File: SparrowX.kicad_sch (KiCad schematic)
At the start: 27 parts, among them J1 NORTH, J2 SOUTH, J3 WEST, J4 EAST, U1 TPS629210-Q1, U2 LD49100PU33RY, U3 STM32G0B1CBU6, U4 TCAN332G, U5 TCAN332G

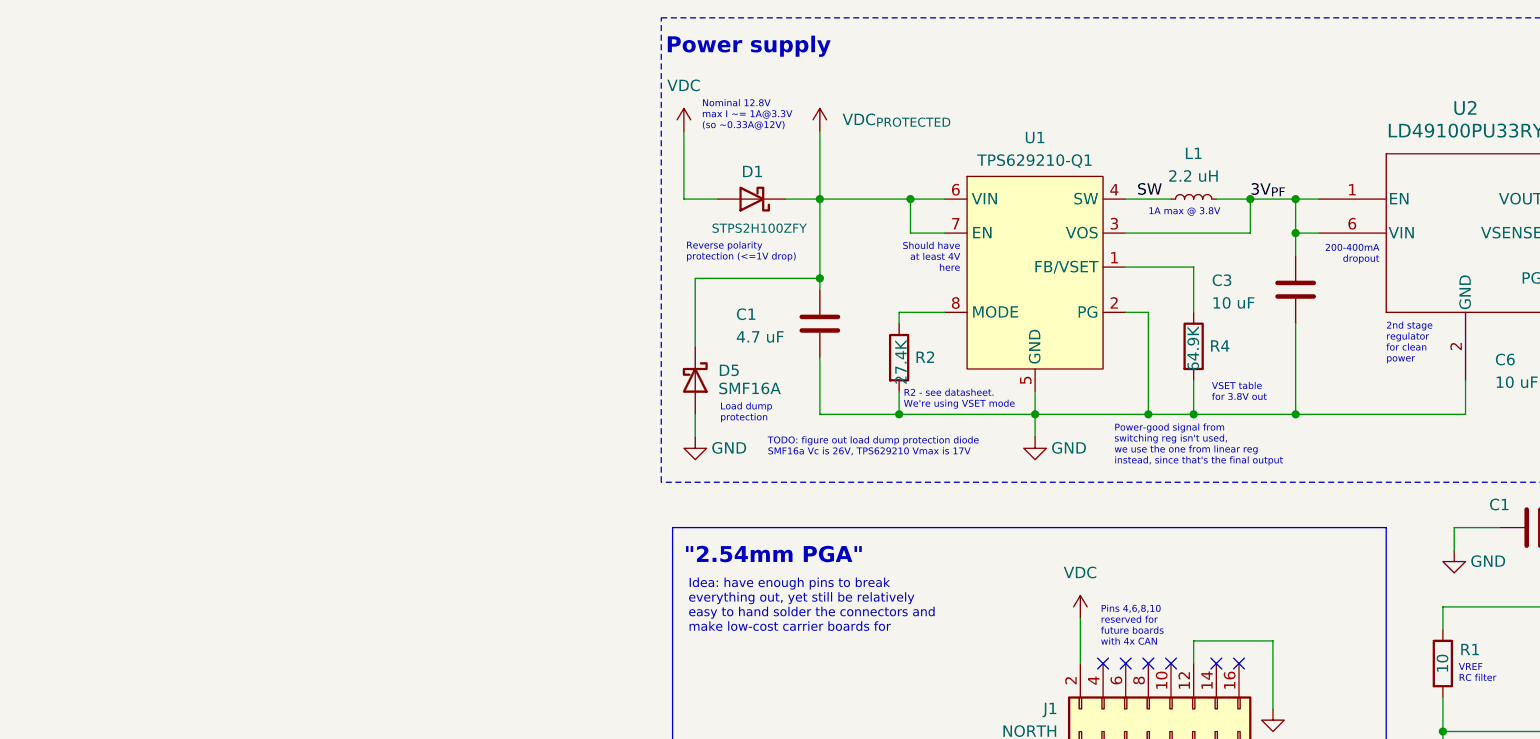
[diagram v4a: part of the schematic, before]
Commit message: WIP: new switching regulator
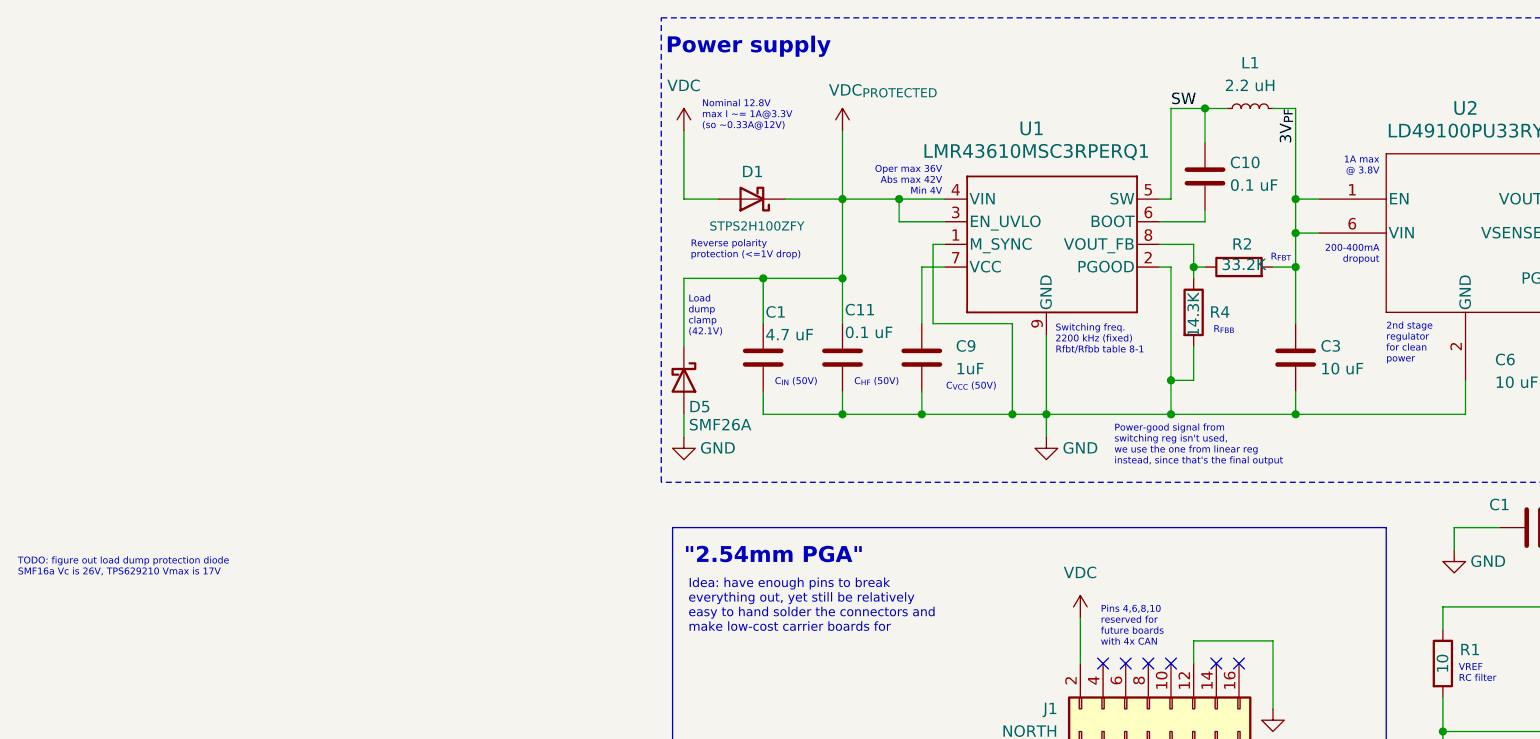
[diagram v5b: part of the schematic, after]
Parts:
- removed U1: TPS629210-Q1, Package_TO_SOT_SMD:SOT-583-8, symbol SparrowX-Components-Library:TPS629210
- added C10, C11: 0.1 uF, Capacitor_SMD:C_0402_1005Metric, symbol Device:C
- added C9: 1uF, Capacitor_SMD:C_0402_1005Metric, symbol Device:C
- added U1: LMR43610MSC3RPERQ1, footprint:RPE0009A-MFG, symbol LMR43610MSC5RPERQ1:LMR43610MSC5RPERQ1
- C3: footprint Capacitor_SMD:C_0805_2012Metric -> Capacitor_SMD:C_0402_1005Metric
- D5: value SMF16A -> SMF26A
- R2: value 27.4K -> 33.2K
- R4: value 64.9K -> 14.3K
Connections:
- net 3V_{PF}: now also R2.2
- net GND: now also C11.2, C9.2, U1.1 (M_SYNC), U1.2 (PGOOD), U1.9 (GND); no longer R2.2
- net SW: now also C10.2, U1.5 (SW)
- net VDC_{PROTECTED}: now also C11.1, U1.3 (EN_UVLO), U1.4 (VIN)
- net at R4.1: now also R2.1, U1.8 (VOUT_FB)
- new net: C10.1, U1.6 (BOOT)
- new net: C9.1, U1.7 (VCC)
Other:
- note added: "C_{HF} (50V)"
- note added: "C_{IN} (50V)"
- note added: "C_{VCC} (50V)"
- note added: "Load dump clamp (42.1V)"
- note added: "Oper max 36V Abs max 42V Min 4V"
- note added: "R_{FBB}"
- note added: "R_{FBT}"
- note added: "Switching freq. 2200 kHz (fixed) Rfbt/Rfbb table 8-1"
- note removed: "Load dump protection"
- note removed: "R2 - see datasheet. We're using VSET mode"
- note removed: "Should have at least 4V here"
- note removed: "VSET table for 3.8V out"
- moved on the sheet: C1, C3, D5, L1, R2, R4

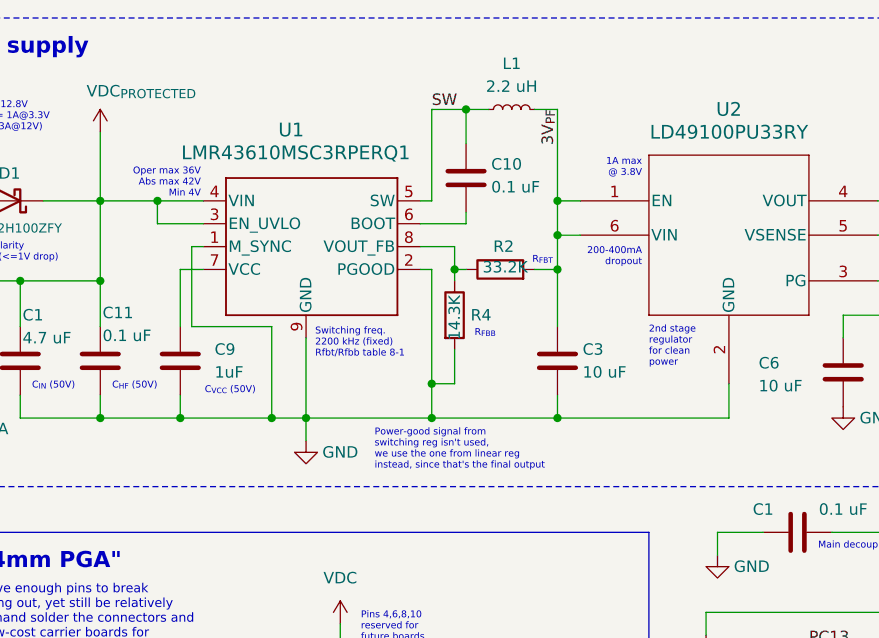
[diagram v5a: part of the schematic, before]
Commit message: PSU P1 migration done!
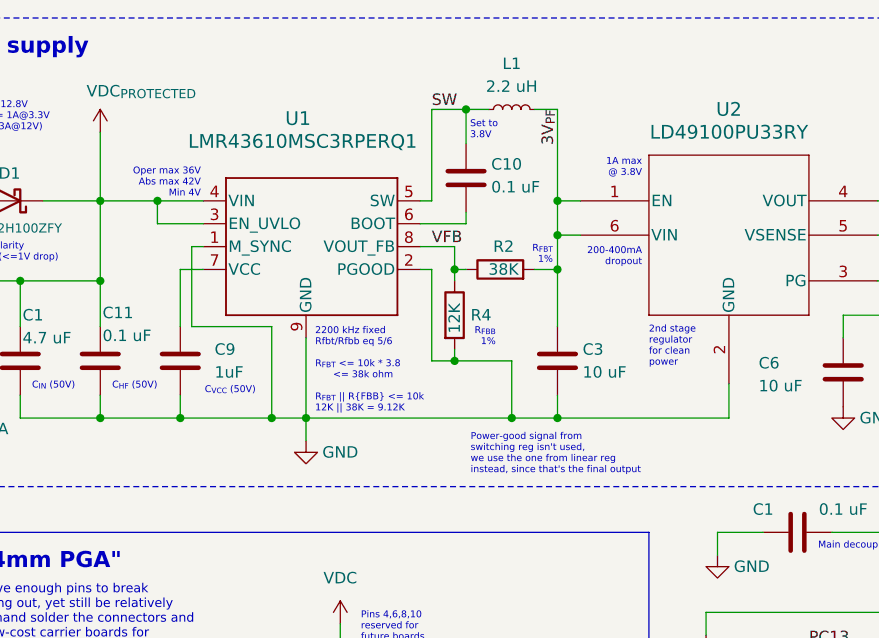
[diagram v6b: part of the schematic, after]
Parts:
- R2: value 33.2K -> 38K
- R4: value 14.3K -> 12K
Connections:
- net VFB: now reaches R2.1, R4.1, U1.8 (VOUT_FB)
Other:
- note added: "2200 kHz fixed Rfbt/Rfbb eq 5/6 R_{FBT} <= 10k * 3.8 <= 38k ohm R_{FBT} || R{FBB} <= 10k 12K || 38K = 9.12K"
- note added: "R_{FBB} 1%"
- note added: "R_{FBT} 1%"
- note added: "Set to 3.8V"
- note removed: "R_{FBB}"
- note removed: "R_{FBT}"
- note removed: "Switching freq. 2200 kHz (fixed) Rfbt/Rfbb table 8-1"
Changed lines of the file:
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@@
 	)
 	(junction
+		(at 72.39 50.8)
+		(diameter 0)
+		(color 0 0 0 0)
+	)
+	(junction
 		(at 123.19 45.72)
 		(diameter 0)
@@
 	)
 	(junction
-		(at 69.85 53.34)
-		(diameter 0)
-		(color 0 0 0 0)
-	)
-	(junction
 		(at 72.39 40.64)
 		(diameter 0)
@@
 	)
 	(junction
+		(at 78.74 57.15)
+		(diameter 0)
+		(color 0 0 0 0)
+	)
+	(junction
 		(at 27.94 130.81)
 		(diameter 0)
@@
 	)
 	(junction
-		(at 69.85 57.15)
-		(diameter 0)
-		(color 0 0 0 0)
-	)
-	(junction
 		(at 232.41 113.03)
 		(diameter 0)
@@
 	(wire
 		(pts
+			(xy 72.39 50.8) (xy 78.74 50.8)
+		)
+		(stroke
+			(width 0)
+			(type default)
+		)
+	)
+	(wire
+		(pts
+			(xy 69.85 50.8) (xy 72.39 50.8)
+		)
+		(stroke
+			(width 0)
+			(type default)
+		)
+	)
+	(wire
+		(pts
 			(xy 45.72 180.34) (xy 45.72 189.23)
 		)
@@
 		)
 	)
+	(wire
+		(pts
+			(xy 78.74 50.8) (xy 78.74 57.15)
+		)
+		(stroke
+			(width 0)
+			(type default)
+		)
+	)
 	(bus
 		(pts
@@
 	(wire
 		(pts
-			(xy 55.88 57.15) (xy 69.85 57.15)
-		)
-		(stroke
-			(width 0)
-			(type default)
-		)
-	)
-	(wire
-		(pts
 			(xy 119.38 36.83) (xy 123.19 36.83)
 		)
@@
 	(wire
 		(pts
-			(xy 69.85 53.34) (xy 69.85 57.15)
-		)
-		(stroke
-			(width 0)
-			(type default)
-		)
-	)
-	(wire
-		(pts
 			(xy 72.39 38.1) (xy 72.39 40.64)
 		)
@@
 	(wire
 		(pts
+			(xy 78.74 57.15) (xy 83.82 57.15)
+		)
+		(stroke
+			(width 0)
+			(type default)
+		)
+	)
+	(wire
+		(pts
 			(xy 160.02 121.92) (xy 160.02 135.89)
 		)
@@
 	(wire
 		(pts
-			(xy 72.39 53.34) (xy 69.85 53.34)
-		)
-		(stroke
-			(width 0)
-			(type default)
-		)
-	)
-	(wire
-		(pts
 			(xy 41.91 40.64) (xy 41.91 46.99)
 		)
@@
 	(wire
 		(pts
-			(xy 69.85 57.15) (xy 83.82 57.15)
+			(xy 55.88 57.15) (xy 78.74 57.15)
 		)
 		(stroke
@@
 	(wire
 		(pts
-			(xy 72.39 49.53) (xy 72.39 53.34)
+			(xy 72.39 49.53) (xy 72.39 50.8)
 		)
 		(stroke
@@
 	(wire
 		(pts
-			(xy 69.85 40.64) (xy 69.85 53.34)
+			(xy 69.85 40.64) (xy 69.85 50.8)
 		)
 		(stroke
@@
 		)
 	)
-	(text "Switching freq.\n2200 kHz (fixed)\nRfbt/Rfbb table 8-1"
+	(text "2200 kHz fixed\nRfbt/Rfbb eq 5/6\n\nR_{FBT} <= 10k * 3.8\n      <= 38k ohm\n\nR_{FBT} || R{FBB} <= 10k\n12K || 38K = 9.12K\n"
 		(exclude_from_sim no)
-		(at 56.896 50.546 0)
+		(at 56.896 56.642 0)
 		(effects
 			(font
@@
 	(text "Power-good signal from\nswitching reg isn't used,\nwe use the one from linear reg\ninstead, since that's the final output"
 		(exclude_from_sim no)
-		(at 63.5 62.992 0)
+		(at 74.168 63.5 0)
 		(effects
 			(font
@@
 		)
 	)
-	(text "R_{FBB}"
+	(text "R_{FBB}\n1%"
 		(exclude_from_sim no)
-		(at 76.962 48.26 0)
+		(at 76.962 49.276 0)
 		(effects
 			(font
@@
 		)
 	)
+	(text "Set to\n3.8V"
+		(exclude_from_sim no)
+		(at 74.1117 26.288 0)
+		(effects
+			(font
+				(size 0.762 0.762)
+			)
+			(justify left bottom)
+		)
+	)
 	(text "USB ESD\nProtection"
 		(exclude_from_sim no)
@@
 		)
 	)
-	(text "R_{FBT}"
+	(text "R_{FBT}\n1%"
 		(exclude_from_sim no)
 		(at 83.312 40.132 0)
@@
 		)
 	)
+	(label "VFB"
+		(at 69.85 38.1 0)
+		(fields_autoplaced yes)
+		(effects
+			(font
+				(size 1.27 1.27)
+			)
+			(justify left bottom)
+		)
+	)
 	(label "PA0"
 		(at 43.18 189.23 90)
@@
 			)
 		)
-		(property "Value" "14.3K"
-			(at 72.39 48.514 90)
+		(property "Value" "12K"
+			(at 72.39 47.752 90)
 			(effects
 				(font
@@
 		(dnp no)
 		(property "Reference" "U1"
-			(at 54.229 25.146 0)
+			(at 54.991 23.876 0)
 			(effects
 				(font
@@
 		)
 		(property "Value" "LMR43610MSC3RPERQ1"
-			(at 54.737 27.686 0)
+			(at 55.499 26.416 0)
 			(effects
 				(font
@@
 			)
 		)
-		(property "Value" "33.2K"
-			(at 80.518 40.386 90)
+		(property "Value" "38K"
+			(at 79.502 40.64 90)
 			(effects
 				(font

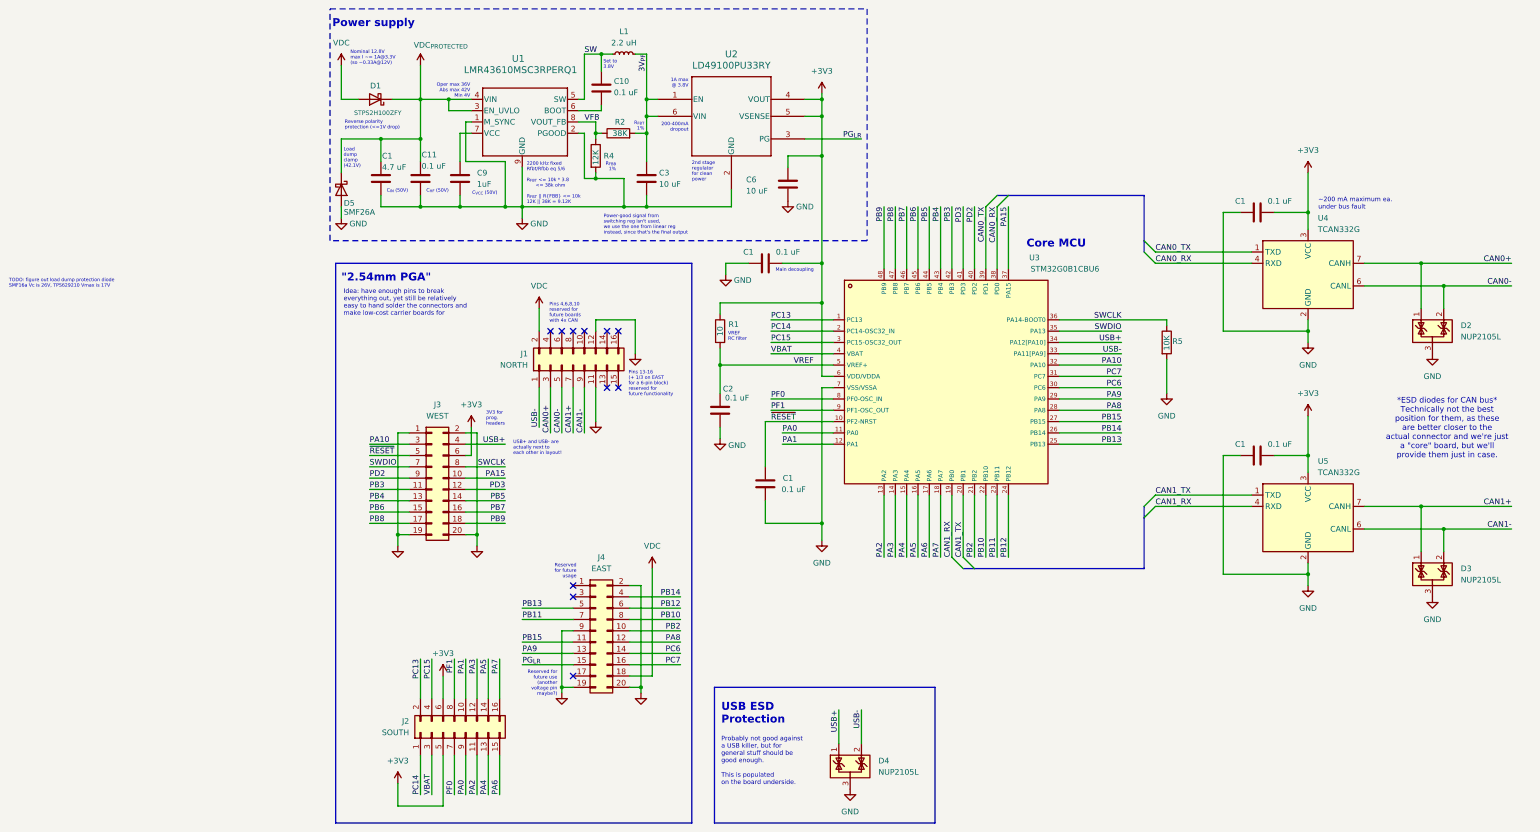
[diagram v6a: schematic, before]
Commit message: Schematic comment touch-ups
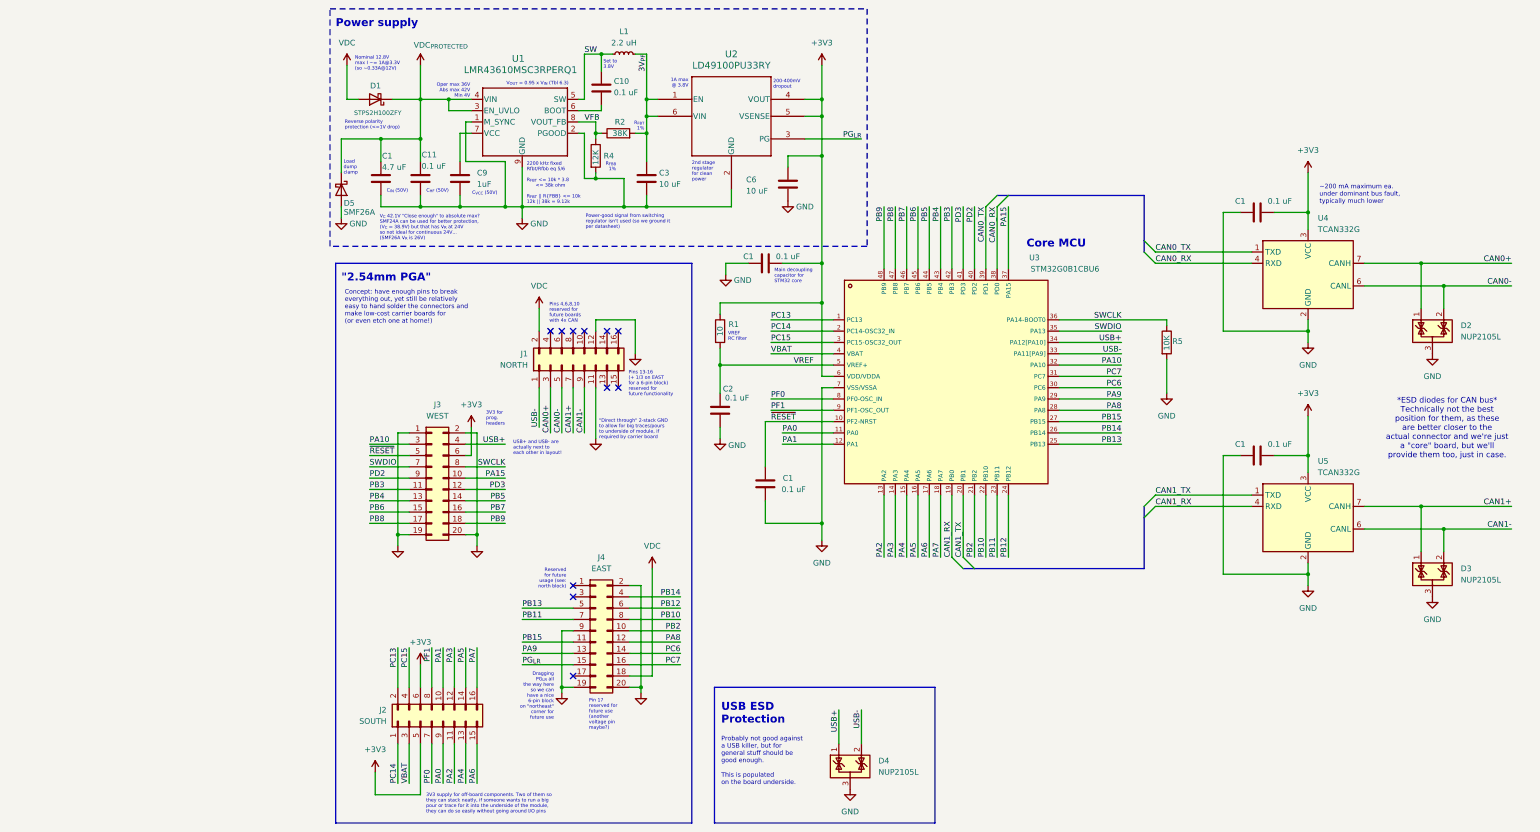
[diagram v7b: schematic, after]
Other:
- note added: ""Direct through" 2-stack GND to allow for big traces/pours to underside of module, if required by carrier board"
- note added: "*ESD diodes for CAN bus* Technically not the best position for them, as these are better closer to the actual connector and we're just a "core" board, but we'll provide them too, just in case."
- note added: "200-400mV dropout"
- note added: "2200 kHz fixed Rfbt/Rfbb eq 5/6 R_{FBT} <= 10k * 3.8 <= 38k ohm R_{FBT} || R{FBB} <= 10k 12k || 38k = 9.12k"
- note added: "3V3 supply for off-board components. Two of them so they can stack neatly, if someone wants to run a big pour or trace for it into the underside of the module, they can do so easily without going around I/O pins"
- note added: "Concept: have enough pins to break everything out, yet still be relatively easy to hand solder the connectors and make low-cost carrier boards for (or even etch one at home!)"
- note added: "Dragging PG_{LR} all the way here so we can have a nice 6-pin block on "northeast" corner for future use"
- note added: "Load dump clamp"
- note added: "Main decoupling capacitor for STM32 core"
- note added: "Pin 17 reserved for future use (another voltage pin maybe?)"
- note added: "Power-good signal from switching regulator isn't used (so we ground it per datasheet)"
- note added: "Reserved for future usage (see: north block)"
- note added: "V_{C} 42.1V "Close enough" to absolute max? SMF24A can be used for better protection, (V_{C} = 38.9V) but that has V_{R} at 24V so not ideal for continuous 24V... (SMF26A V_{R} is 26V)"
- note added: "V_{OUT} = 0.95 x V_{IN} (Tbl 6.3)"
- note added: "~200 mA maximum ea. under dominant bus fault, typically much lower"
- note removed: "*ESD diodes for CAN bus* Technically not the best position for them, as these are better closer to the actual connector and we're just a "core" board, but we'll provide them just in case."
- note removed: "200-400mA dropout"
- note removed: "2200 kHz fixed Rfbt/Rfbb eq 5/6 R_{FBT} <= 10k * 3.8 <= 38k ohm R_{FBT} || R{FBB} <= 10k 12K || 38K = 9.12K"
- note removed: "Idea: have enough pins to break everything out, yet still be relatively easy to hand solder the connectors and make low-cost carrier boards for"
- note removed: "Load dump clamp (42.1V)"
- note removed: "Main decoupling"
- note removed: "Power-good signal from switching reg isn't used, we use the one from linear reg instead, since that's the final output"
- note removed: "Reserved for future usage"
- note removed: "Reserved for future use (another voltage pin maybe?)"
- note removed: "TODO: figure out load dump protection diode SMF16a Vc is 26V, TPS629210 Vmax is 17V"
- note removed: "~200 mA maximum ea. under bus fault"
- title: tinySPARROW NG ECU core board -> tinySPARROW 2 ECU core board
- moved on the sheet: J2
